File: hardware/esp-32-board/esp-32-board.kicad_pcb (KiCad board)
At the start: 2 copper layers, 53.4 x 68.6 mm, 37 parts, among them J1 ESP-PROG-Program, J2 MainConnector, J3 ESP-PROG-Debug, J4 Conn_01x06, J5 Barrel_Jack_MountingPin, J6 Conn_01x02, J7 USB_B_Micro, Q1 BCR129S, SW1 SW_Push, SW2 SW_Push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

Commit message: Swap RX and TX on FT232RL
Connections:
- U5 pad 1: /TXD0 -> /RXD0
- U5 pad 5: /RXD0 -> /TXD0
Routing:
- net /RXD0: track 76.2 -> 70.6 mm
- net /TXD0: track 79.1 -> 75.4 mm

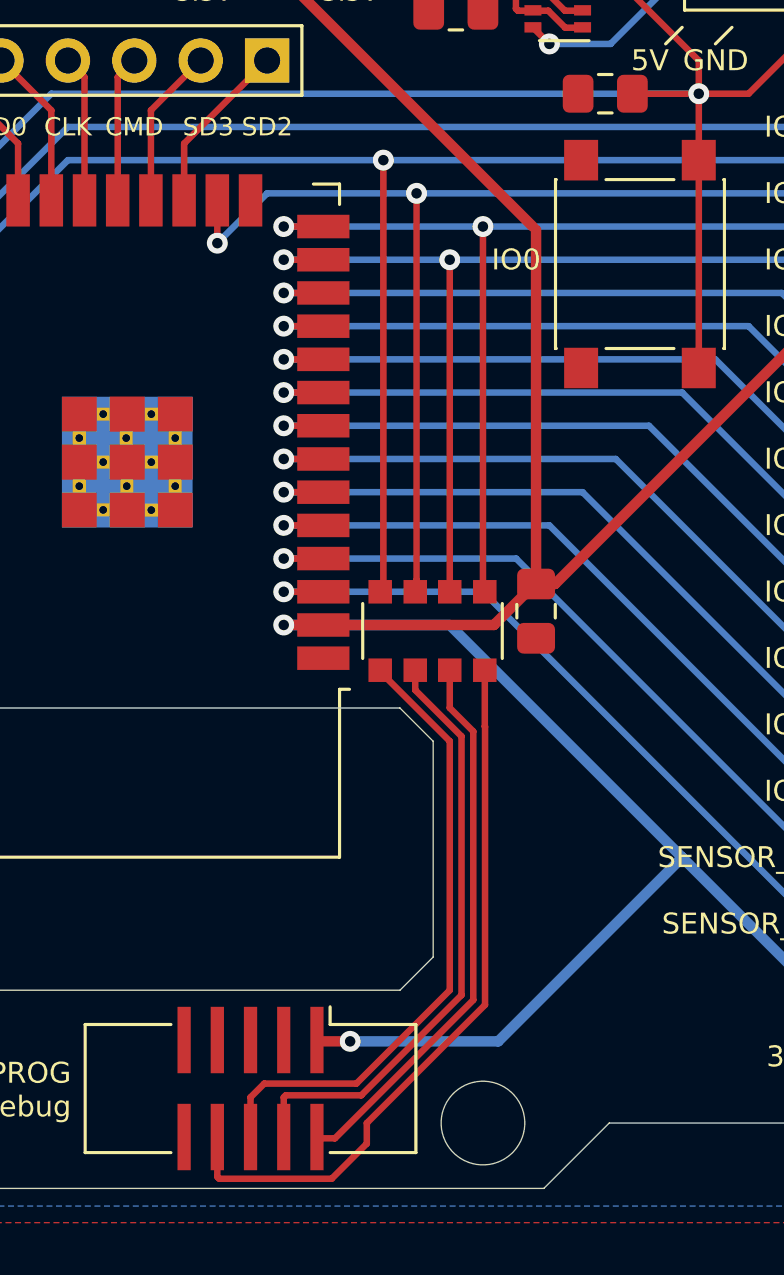
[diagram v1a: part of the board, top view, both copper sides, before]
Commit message: Use 1206 resistor array for RN1
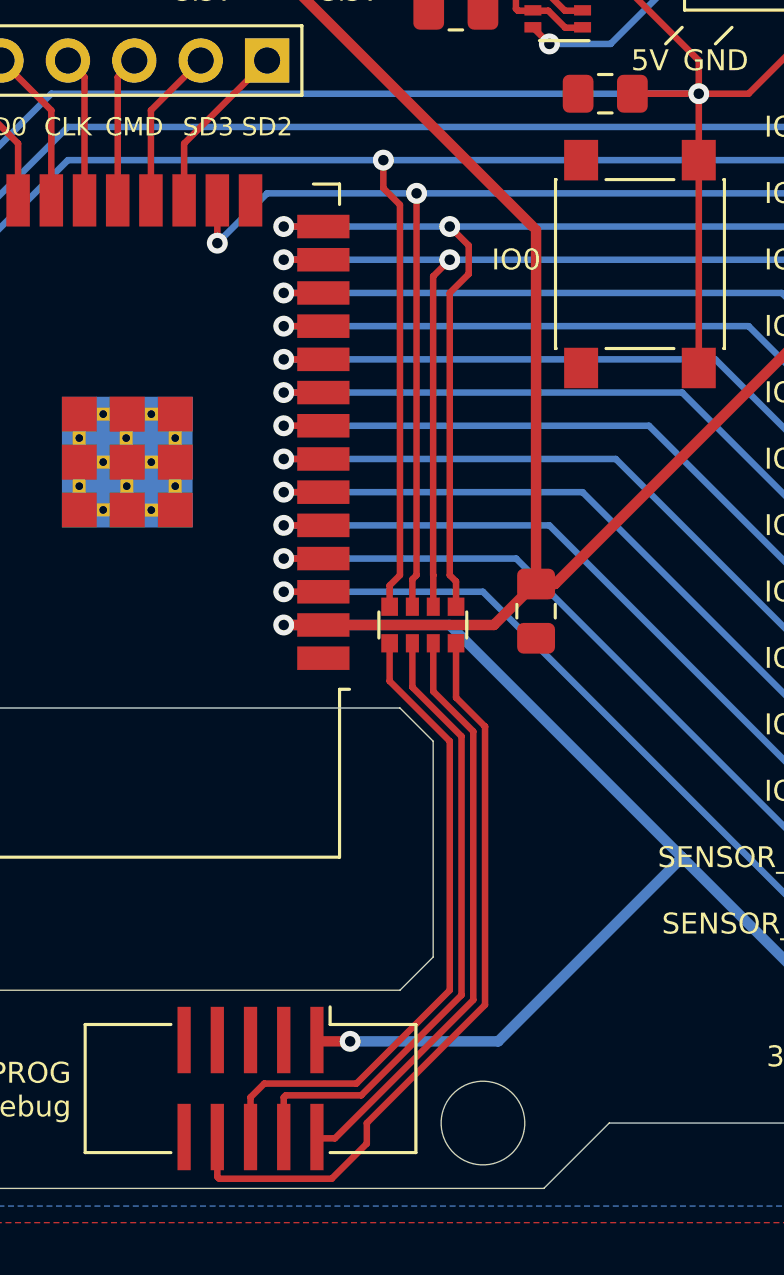
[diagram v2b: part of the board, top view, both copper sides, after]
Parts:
- RN1: footprint Resistor_SMD:R_Array_Convex_4x1206 -> Resistor_SMD:R_Array_Convex_4x0612
- moved RN1 0.44 mm to (162.8, 68.6)
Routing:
- net Net-(J3-Pad8): track 27.8 -> 29.3 mm
- net Net-(J3-Pad2): track 21.2 -> 22.4 mm
- net /IO12: track 38.9 -> 40.1 mm
- net Net-(J3-Pad4): track 23.1 -> 24.2 mm
- net /IO15: track 54.3 -> 55.3 mm
- net Net-(J3-Pad6): track 24.2 -> 25.1 mm
- net /IO14: track 38.1 -> 39.0 mm

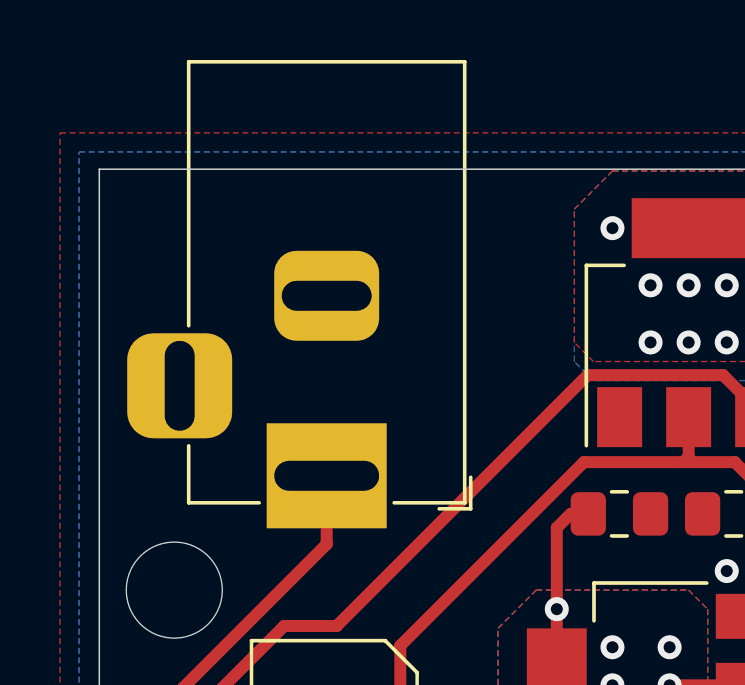
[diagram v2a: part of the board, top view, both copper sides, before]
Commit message: Change DC connector to CLIFF FC68148
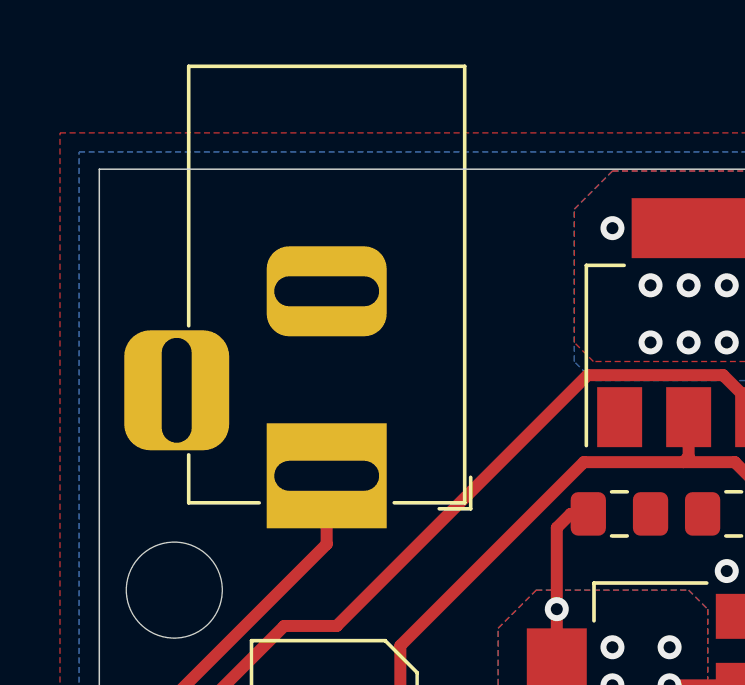
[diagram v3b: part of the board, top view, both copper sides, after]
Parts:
- J5: footprint Connector_BarrelJack:BarrelJack_Lumberg_1613-21_Horizontal -> Connector_BarrelJack:BarrelJack_CLIFF_FC68148_Horizontal
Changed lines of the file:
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@@
     (add_net "Net-(D4-Pad1)")
     (add_net "Net-(D5-Pad1)")
+    (add_net "Net-(J3-Pad10)")
     (add_net "Net-(J3-Pad2)")
     (add_net "Net-(J3-Pad4)")
@@
     (add_net "Net-(J3-Pad8)")
     (add_net "Net-(R2-Pad1)")
+    (add_net "Net-(U1-Pad32)")
+    (add_net "Net-(U5-Pad10)")
+    (add_net "Net-(U5-Pad11)")
+    (add_net "Net-(U5-Pad12)")
+    (add_net "Net-(U5-Pad13)")
+    (add_net "Net-(U5-Pad14)")
+    (add_net "Net-(U5-Pad27)")
+    (add_net "Net-(U5-Pad28)")
+    (add_net "Net-(U5-Pad6)")
+    (add_net "Net-(U5-Pad9)")
   )
   (net_class Power ""
@@
     (add_net "Net-(J7-Pad2)")
     (add_net "Net-(J7-Pad3)")
+  )
+  (module Connector_BarrelJack:BarrelJack_CLIFF_FC68148_Horizontal (layer F.Cu)
+    (at 137.16 31.75 270)
+    (descr "DC Barrel Jack")
+    (tags "Power Jack")
+    (fp_text reference J5 (at -9.652 5.334 180) (layer F.SilkS) hide
+      (effects (font (size 0.6 0.6) (thickness 0.15)))
+    )
+    (fp_text value Barrel_Jack_MountingPin (at -8.636 0 180) (layer F.Fab)
+      (effects (font (size 0.3 0.3) (thickness 0.05)))
+    )
+    (fp_text user %R (at -3.048 0.762 180) (layer F.Fab)
+      (effects (font (size 1 1) (thickness 0.15)))
+    )
+    (fp_line (start -0.003213 -4.505425) (end 0.8 -3.75) (layer F.Fab) (width 0.1))
+    (fp_line (start 1.1 -3.75) (end 1.1 -4.8) (layer F.SilkS) (width 0.12))
+    (fp_line (start 0.05 -4.8) (end 1.1 -4.8) (layer F.SilkS) (width 0.12))
+    (fp_line (start 1 -4.5) (end 1 -4.75) (layer F.CrtYd) (width 0.05))
+    (fp_line (start 1 -4.75) (end -14 -4.75) (layer F.CrtYd) (width 0.05))
+    (fp_line (start 1 -4.5) (end 1 -2.25) (layer F.CrtYd) (width 0.05))
+    (fp_line (start 1 -2.25) (end 2 -2.25) (layer F.CrtYd) (width 0.05))
+    (fp_line (start 2 -2.25) (end 2 2.25) (layer F.CrtYd) (width 0.05))
+    (fp_line (start 2 2.25) (end 1 2.25) (layer F.CrtYd) (width 0.05))
+    (fp_line (start 1 2.25) (end 1 4.75) (layer F.CrtYd) (width 0.05))
+    (fp_line (start 1 4.75) (end -0.7 4.75) (layer F.CrtYd) (width 0.05))
+    (fp_line (start -0.7 4.75) (end -0.7 6.95) (layer F.CrtYd) (width 0.05))
+    (fp_line (start -0.7 6.95) (end -5 6.95) (layer F.CrtYd) (width 0.05))
+    (fp_line (start -5 6.95) (end -5 4.75) (layer F.CrtYd) (width 0.05))
+    (fp_line (start -5 4.75) (end -14 4.75) (layer F.CrtYd) (width 0.05))
+    (fp_line (start -14 4.75) (end -14 -4.75) (layer F.CrtYd) (width 0.05))
+    (fp_line (start -5 4.6) (end -13.65 4.6) (layer F.SilkS) (width 0.12))
+    (fp_line (start -13.65 4.6) (end -13.65 -4.6) (layer F.SilkS) (width 0.12))
+    (fp_line (start 0.9 2.25) (end 0.9 4.6) (layer F.SilkS) (width 0.12))
+    (fp_line (start 0.9 4.6) (end -0.7 4.6) (layer F.SilkS) (width 0.12))
+    (fp_line (start -13.65 -4.6) (end 0.9 -4.6) (layer F.SilkS) (width 0.12))
+    (fp_line (start 0.9 -4.6) (end 0.9 -2.25) (layer F.SilkS) (width 0.12))
+    (fp_line (start -10.5 -4.5) (end -10.5 4.5) (layer F.Fab) (width 0.1))
+    (fp_line (start -13.55 -4.5) (end -13.55 4.5) (layer F.Fab) (width 0.1))
+    (fp_line (start -13.55 4.5) (end 0.8 4.5) (layer F.Fab) (width 0.1))
+    (fp_line (start 0.8 4.5) (end 0.8 -3.75) (layer F.Fab) (width 0.1))
+    (fp_line (start 0 -4.5) (end -13.55 -4.5) (layer F.Fab) (width 0.1))
+    (pad 1 thru_hole rect (at 0 0 270) (size 3.5 4) (drill oval 1 3.5) (layers *.Cu *.Mask)
+      (net 43 "Net-(D2-Pad2)"))
+    (pad 2 thru_hole roundrect (at -6.15 0 270) (size 3 4) (drill oval 1 3.5) (layers *.Cu *.Mask) (roundrect_rratio 0.25)
+      (net 1 GND))
+    (pad 3 thru_hole roundrect (at -2.85 5 270) (size 4 3.5) (drill oval 3.5 1) (layers *.Cu *.Mask) (roundrect_rratio 0.25)
+      (net 1 GND))
+    (model ${KISYS3DMOD}/Connector_BarrelJack.3dshapes/BarrelJack_CLIFF_FC68148_Horizontal.wrl
+      (at (xyz 0 0 0))
+      (scale (xyz 1 1 1))
+      (rotate (xyz 0 0 0))
+    )
   )
   (module Resistor_SMD:R_Array_Convex_4x0612 (layer F.Cu)
@@
       (at (xyz 0 0 0))
       (scale (xyz 1 1 1))
-      (rotate (xyz 0 0 0))
-    )
-  )
-  (module Connector_BarrelJack:BarrelJack_Lumberg_1613-21_Horizontal (layer F.Cu)
-    (at 137.16 31.75 270)
-    (descr "DC Barrel Jack")
-    (tags "Power Jack")
-    (fp_text reference J5 (at -9.652 5.334 180) (layer F.SilkS) hide
-      (effects (font (size 0.6 0.6) (thickness 0.15)))
-    )
-    (fp_text value Barrel_Jack_MountingPin (at -8.636 0 180) (layer F.Fab)
-      (effects (font (size 0.3 0.3) (thickness 0.05)))
-    )
-    (fp_line (start 0 -4.5) (end -13.7 -4.5) (layer F.Fab) (width 0.1))
-    (fp_line (start 0.8 4.5) (end 0.8 -3.75) (layer F.Fab) (width 0.1))
-    (fp_line (start -13.7 4.5) (end 0.8 4.5) (layer F.Fab) (width 0.1))
-    (fp_line (start -13.7 -4.5) (end -13.7 4.5) (layer F.Fab) (width 0.1))
-    (fp_line (start -10.2 -4.5) (end -10.2 4.5) (layer F.Fab) (width 0.1))
-    (fp_line (start 0.9 -4.6) (end 0.9 -2.25) (layer F.SilkS) (width 0.12))
-    (fp_line (start -13.8 -4.6) (end 0.9 -4.6) (layer F.SilkS) (width 0.12))
-    (fp_line (start 0.9 4.6) (end -1 4.6) (layer F.SilkS) (width 0.12))
-    (fp_line (start 0.9 2.25) (end 0.9 4.6) (layer F.SilkS) (width 0.12))
-    (fp_line (start -13.8 4.6) (end -13.8 -4.6) (layer F.SilkS) (width 0.12))
-    (fp_line (start -5 4.6) (end -13.8 4.6) (layer F.SilkS) (width 0.12))
-    (fp_line (start -14 4.75) (end -14 -4.75) (layer F.CrtYd) (width 0.05))
-    (fp_line (start -5 4.75) (end -14 4.75) (layer F.CrtYd) (width 0.05))
-    (fp_line (start -5 6.95) (end -5 4.75) (layer F.CrtYd) (width 0.05))
-    (fp_line (start -1 6.95) (end -5 6.95) (layer F.CrtYd) (width 0.05))
-    (fp_line (start -1 4.75) (end -1 6.95) (layer F.CrtYd) (width 0.05))
-    (fp_line (start 1 4.75) (end -1 4.75) (layer F.CrtYd) (width 0.05))
-    (fp_line (start 1 2.25) (end 1 4.75) (layer F.CrtYd) (width 0.05))
-    (fp_line (start 2 2.25) (end 1 2.25) (layer F.CrtYd) (width 0.05))
-    (fp_line (start 2 -2.25) (end 2 2.25) (layer F.CrtYd) (width 0.05))
-    (fp_line (start 1 -2.25) (end 2 -2.25) (layer F.CrtYd) (width 0.05))
-    (fp_line (start 1 -4.5) (end 1 -2.25) (layer F.CrtYd) (width 0.05))
-    (fp_line (start 1 -4.75) (end -14 -4.75) (layer F.CrtYd) (width 0.05))
-    (fp_line (start 1 -4.5) (end 1 -4.75) (layer F.CrtYd) (width 0.05))
-    (fp_line (start 0.05 -4.8) (end 1.1 -4.8) (layer F.SilkS) (width 0.12))
-    (fp_line (start 1.1 -3.75) (end 1.1 -4.8) (layer F.SilkS) (width 0.12))
-    (fp_line (start -0.003213 -4.505425) (end 0.8 -3.75) (layer F.Fab) (width 0.1))
-    (fp_text user %R (at -3.048 0.762 180) (layer F.Fab)
-      (effects (font (size 1 1) (thickness 0.15)))
-    )
-    (pad 3 thru_hole roundrect (at -3 4.9 270) (size 3.5 3.5) (drill oval 3 1) (layers *.Cu *.Mask) (roundrect_rratio 0.25)
-      (net 1 GND))
-    (pad 2 thru_hole roundrect (at -6 0 270) (size 3 3.5) (drill oval 1 3) (layers *.Cu *.Mask) (roundrect_rratio 0.25)
-      (net 1 GND))
-    (pad 1 thru_hole rect (at 0 0 270) (size 3.5 4) (drill oval 1 3.5) (layers *.Cu *.Mask)
-      (net 43 "Net-(D2-Pad2)"))
-    (model ${KISYS3DMOD}/Connector_BarrelJack.3dshapes/BarrelJack_Lumberg_1613-21_Horizontal.wrl
-      (at (xyz 0 0 0))
-      (scale (xyz 1 1 1))

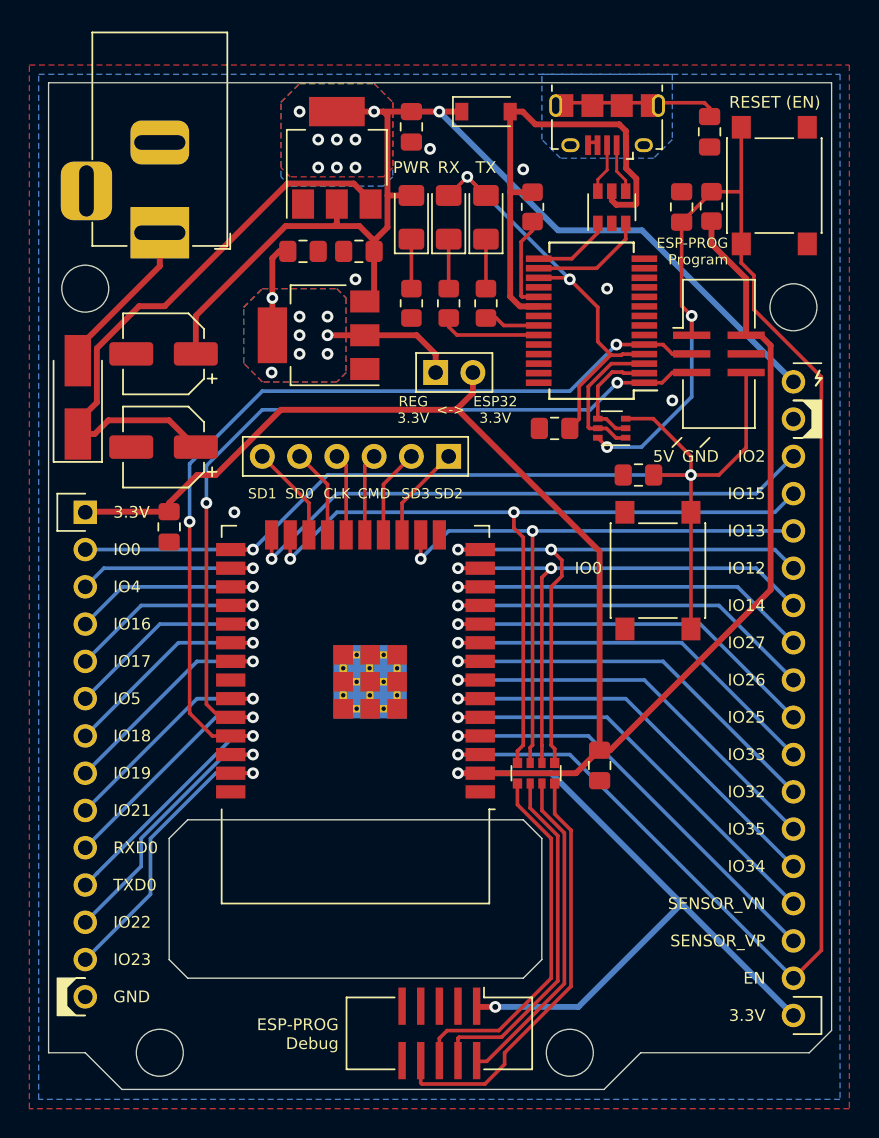
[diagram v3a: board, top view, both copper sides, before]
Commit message: Remove power switch
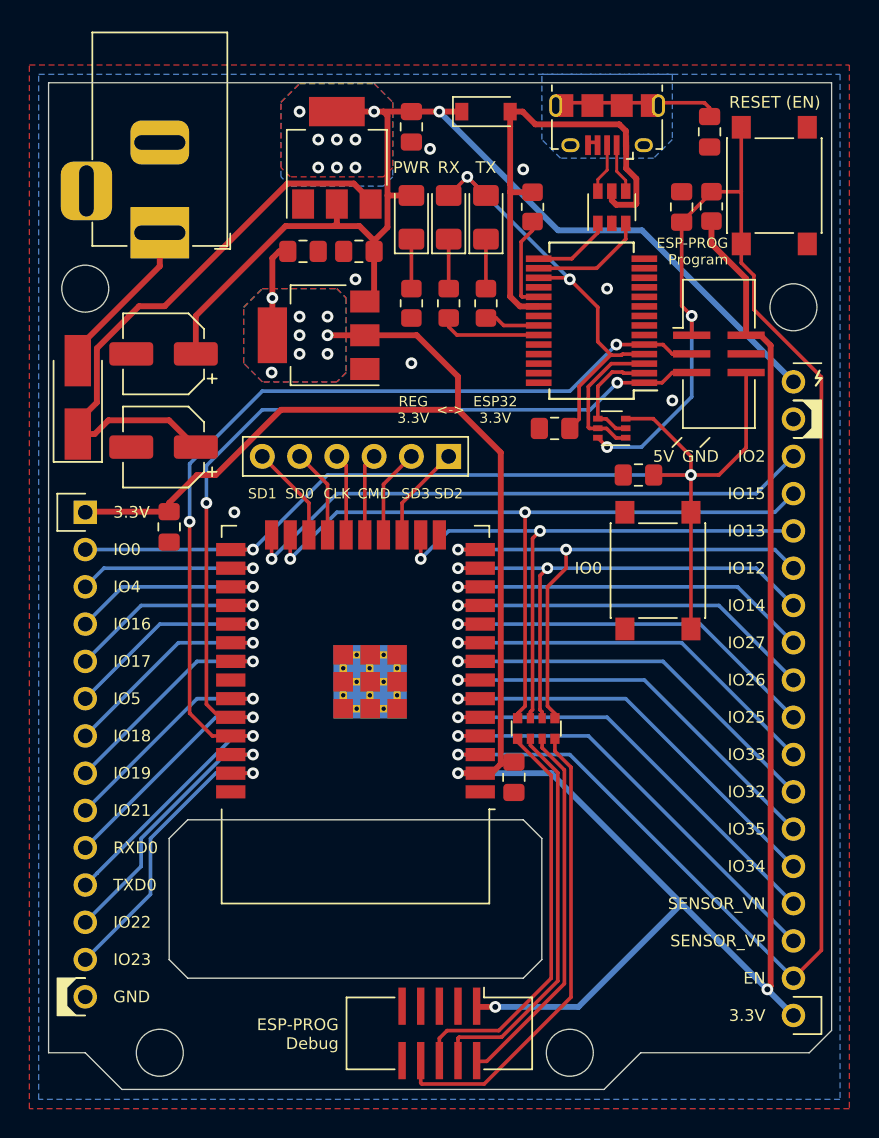
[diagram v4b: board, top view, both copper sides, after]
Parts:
- removed J6: Conn_01x02, Connector_PinHeader_2.54mm:PinHeader_1x02_P2.54mm_Vertical
- moved C1 5.90 mm to (161.3, 68.9)
- moved RN1 3.05 mm to (162.8, 65.5)
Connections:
- C6 pad 1: /Power/Internal_3V3 -> +3V3
- U2 pad 2: /Power/Internal_3V3 -> +3V3
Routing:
- net +3V3: track 159.5 -> 178.2 mm, vias 2 -> 11
- net /Power/Internal_3V3: track 15.6 -> 0.00 mm, vias 8 -> 0
- net /IO15: track 55.3 -> 52.0 mm
- net Net-(J3-Pad2): track 22.4 -> 25.5 mm
- net /IO14: track 39.0 -> 35.9 mm
- net Net-(J3-Pad6): track 25.1 -> 28.1 mm
- net Net-(J3-Pad4): track 24.2 -> 27.2 mm
- net /IO12: track 40.1 -> 37.1 mm
- net Net-(J3-Pad8): track 29.3 -> 32.3 mm
- net /IO13: track 43.7 -> 40.9 mm
- net GND: vias 6 -> 7
- added copper zone on B.Cu, net +3V3
- added copper zone on F.Cu, net +3V3
- removed copper zone on B.Cu, net /Power/Internal_3V3
- removed copper zone on F.Cu, net /Power/Internal_3V3

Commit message: Move ESP-PROG ports
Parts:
- moved J1 55.6 mm to (143.1, 84.5), turned to 90 degrees
- moved C2 27.7 mm to (167.0, 75.8), turned to 270 degrees
- moved SW1 26.9 mm to (170.7, 81.6), turned to 180 degrees
- moved Q1 6.85 mm to (173.7, 41.3), turned to 0 degrees
- moved J3 4.84 mm to (154.1, 84.5), turned to 90 degrees
- moved RN1 2.73 mm to (162.8, 62.8)
- moved U1 2.54 mm to (150.5, 59.1)
- moved C1 2.30 mm to (161.5, 66.6)
- moved J4 1.91 mm to (156.8, 45.1)
- moved C11 0.63 mm to (164.7, 45.1)
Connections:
- net /SENSOR_VN renamed /IO39
- net /SENSOR_VP renamed /IO36
- RN1 pad 1: Net-(J3-Pad6) -> Net-(J3-Pad8)
- RN1 pad 2: Net-(J3-Pad4) -> Net-(J3-Pad6)
- RN1 pad 3: Net-(J3-Pad2) -> Net-(J3-Pad4)
- RN1 pad 4: Net-(J3-Pad8) -> Net-(J3-Pad2)
- RN1 pad 5: /IO12 -> /IO14
- RN1 pad 6: /IO14 -> /IO13
- RN1 pad 7: /IO13 -> /IO15
- RN1 pad 8: /IO15 -> /IO12
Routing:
- net /IO0: track 74.4 -> 143.4 mm, vias 2 -> 4
- net /EN: track 118.3 -> 152.1 mm
- net +3V3: track 178.2 -> 205.9 mm, vias 11 -> 12
- net /RXD0: track 70.6 -> 94.1 mm
- net Net-(J3-Pad2): track 25.5 -> 42.7 mm
- net /TXD0: track 75.4 -> 92.6 mm
- net Net-(J3-Pad4): track 27.2 -> 42.7 mm
- net /USB/RTS: track 10.1 -> 4.72 mm
- net Net-(J3-Pad8): track 32.3 -> 28.1 mm
- net VDC: track 39.6 -> 35.7 mm
- net /IO22: track 18.8 -> 22.1 mm
- net /USB/DTR: track 7.99 -> 4.72 mm
- net /IO23: track 20.4 -> 22.8 mm
- net Net-(J3-Pad6): track 28.1 -> 29.8 mm
- net /IO13: track 40.9 -> 42.1 mm
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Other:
- outline, holes or cut-outs redrawn
- board text added: "ESP-PROG"
- board text added: "IO36"
- board text added: "IO39"
- board text removed: "ESP-PROG Debug"
- board text removed: "ESP-PROG Program"
- board text removed: "ESP32 3.3V"
- board text removed: "REG 3.3V"
- board text removed: "SENSOR_VN"
- board text removed: "SENSOR_VP"
